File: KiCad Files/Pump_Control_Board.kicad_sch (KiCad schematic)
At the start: 70 parts, among them J1 OLED, J2 Conn_01x06, J3 USB_C_Receptacle_USB2.0, J4 Jack, M1 Stepper_Motor_bipolar, Q1 SSM3J328R, SW1 SW_USER, SW2 SW_RESET, U1 ESDALD05, U2 SN74LV1T34DCK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

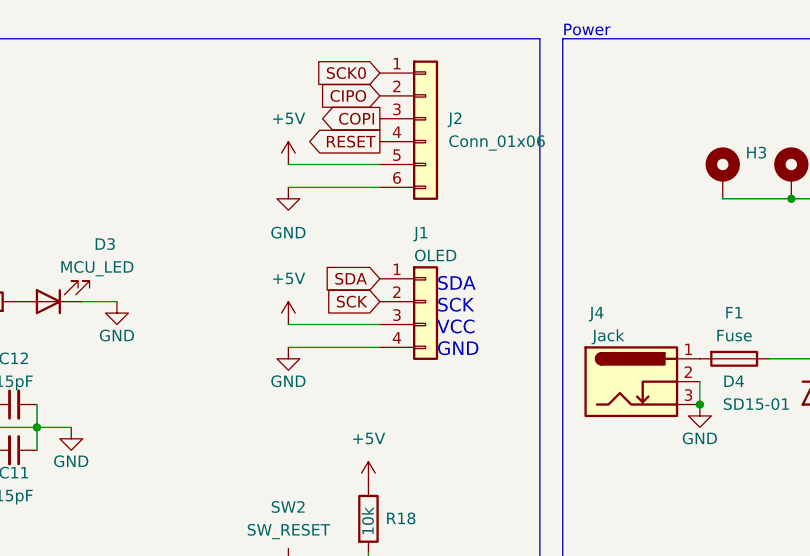
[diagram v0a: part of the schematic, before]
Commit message: Named ICP Header
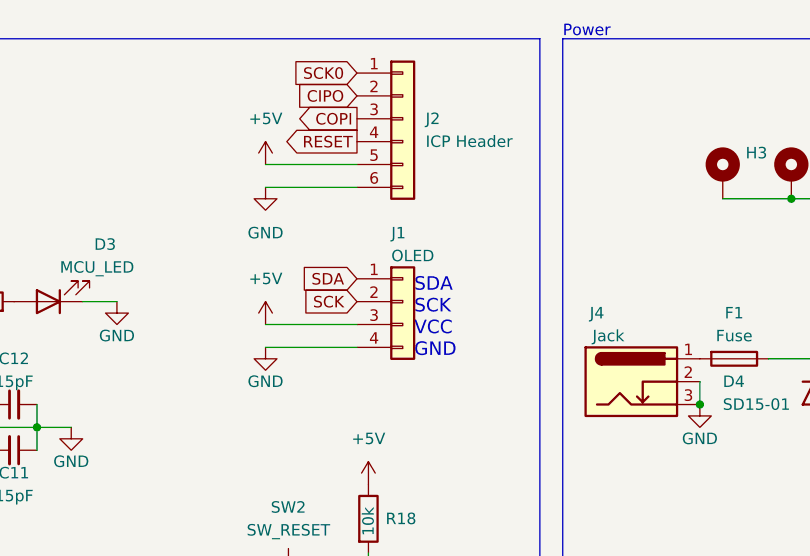
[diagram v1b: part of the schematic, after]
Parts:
- J2: value Conn_01x06 -> ICP Header
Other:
- moved on the sheet: J1, J2
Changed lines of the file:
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@@
     (stroke (width 0) (type default))
   )
-  (wire (pts (xy 107.95 29.21) (xy 118.11 29.21))
+  (wire (pts (xy 105.41 29.21) (xy 115.57 29.21))
     (stroke (width 0) (type default))
   )
@@
     (stroke (width 0) (type default))
   )
-  (wire (pts (xy 107.95 31.75) (xy 118.11 31.75))
+  (wire (pts (xy 105.41 31.75) (xy 115.57 31.75))
     (stroke (width 0) (type default))
   )
@@
     (stroke (width 0) (type default))
   )
-  (wire (pts (xy 107.95 49.53) (xy 118.11 49.53))
+  (wire (pts (xy 105.41 49.53) (xy 115.57 49.53))
     (stroke (width 0) (type default))
   )
@@
     (stroke (width 0) (type default))
   )
-  (wire (pts (xy 107.95 46.99) (xy 118.11 46.99))
+  (wire (pts (xy 105.41 46.99) (xy 115.57 46.99))
     (stroke (width 0) (type default))
   )
@@
     (effects (font (size 5 5)) (justify left bottom))
   )
-  (text "SDA\nSCK\nVCC\nGND" (at 124.46 50.8 0)
+  (text "SDA\nSCK\nVCC\nGND" (at 121.92 50.8 0)
     (effects (font (size 1.5 1.5)) (justify left bottom))
   )
@@
     )
   )
-  (global_label "SCK0" (shape input) (at 118.11 19.05 180) (fields_autoplaced)
+  (global_label "SCK0" (shape input) (at 115.57 19.05 180) (fields_autoplaced)
     (effects (font (size 1.27 1.27)) (justify right))
-    (property "Intersheetrefs" "${INTERSHEET_REFS}" (at 110.1658 19.05 0)
+    (property "Intersheetrefs" "${INTERSHEET_REFS}" (at 107.6258 19.05 0)
       (effects (font (size 1.27 1.27)) (justify right) hide)
     )
@@
     )
   )
-  (global_label "CIPO" (shape input) (at 118.11 21.59 180) (fields_autoplaced)
+  (global_label "CIPO" (shape input) (at 115.57 21.59 180) (fields_autoplaced)
     (effects (font (size 1.27 1.27)) (justify right))
-    (property "Intersheetrefs" "${INTERSHEET_REFS}" (at 110.6495 21.59 0)
+    (property "Intersheetrefs" "${INTERSHEET_REFS}" (at 108.1095 21.59 0)
       (effects (font (size 1.27 1.27)) (justify right) hide)
     )
@@
     )
   )
-  (global_label "SCK" (shape input) (at 118.11 44.45 180) (fields_autoplaced)
+  (global_label "SCK" (shape input) (at 115.57 44.45 180) (fields_autoplaced)
     (effects (font (size 1.27 1.27)) (justify right))
-    (property "Intersheetrefs" "${INTERSHEET_REFS}" (at 111.3753 44.45 0)
+    (property "Intersheetrefs" "${INTERSHEET_REFS}" (at 108.8353 44.45 0)
       (effects (font (size 1.27 1.27)) (justify right) hide)
     )
   )
-  (global_label "COPI" (shape output) (at 118.11 24.13 180) (fields_autoplaced)
+  (global_label "COPI" (shape output) (at 115.57 24.13 180) (fields_autoplaced)
     (effects (font (size 1.27 1.27)) (justify right))
-    (property "Intersheetrefs" "${INTERSHEET_REFS}" (at 110.6495 24.13 0)
+    (property "Intersheetrefs" "${INTERSHEET_REFS}" (at 108.1095 24.13 0)
       (effects (font (size 1.27 1.27)) (justify right) hide)
     )
@@
     )
   )
-  (global_label "RESET" (shape output) (at 118.11 26.67 180) (fields_autoplaced)
+  (global_label "RESET" (shape output) (at 115.57 26.67 180) (fields_autoplaced)
     (effects (font (size 1.27 1.27)) (justify right))
-    (property "Intersheetrefs" "${INTERSHEET_REFS}" (at 109.3797 26.67 0)
+    (property "Intersheetrefs" "${INTERSHEET_REFS}" (at 106.8397 26.67 0)
       (effects (font (size 1.27 1.27)) (justify right) hide)
     )
   )
-  (global_label "SDA" (shape input) (at 118.11 41.91 180) (fields_autoplaced)
+  (global_label "SDA" (shape input) (at 115.57 41.91 180) (fields_autoplaced)
     (effects (font (size 1.27 1.27)) (justify right))
-    (property "Intersheetrefs" "${INTERSHEET_REFS}" (at 111.5567 41.91 0)
+    (property "Intersheetrefs" "${INTERSHEET_REFS}" (at 109.0167 41.91 0)
       (effects (font (size 1.27 1.27)) (justify right) hide)
     )
@@
     )
   )
-  (symbol (lib_id "power:GND") (at 107.95 49.53 0) (unit 1)
+  (symbol (lib_id "power:GND") (at 105.41 49.53 0) (unit 1)
     (in_bom yes) (on_board yes) (dnp no)
-    (property "Reference" "#PWR021" (at 107.95 55.88 0)
+    (property "Reference" "#PWR021" (at 105.41 55.88 0)
       (effects (font (size 1.27 1.27)) hide)
     )
-    (property "Value" "GND" (at 107.95 53.34 0)
+    (property "Value" "GND" (at 105.41 53.34 0)
       (effects (font (size 1.27 1.27)))
     )
-    (property "Footprint" "" (at 107.95 49.53 0)
+    (property "Footprint" "" (at 105.41 49.53 0)
       (effects (font (size 1.27 1.27)) hide)
     )
-    (property "Datasheet" "" (at 107.95 49.53 0)
+    (property "Datasheet" "" (at 105.41 49.53 0)
       (effects (font (size 1.27 1.27)) hide)
     )
@@
     )
   )
-  (symbol (lib_id "Connector_Generic:Conn_01x06") (at 123.19 24.13 0) (unit 1)
+  (symbol (lib_id "Connector_Generic:Conn_01x06") (at 120.65 24.13 0) (unit 1)
     (in_bom yes) (on_board yes) (dnp no) (fields_autoplaced)
-    (property "Reference" "J2" (at 125.73 24.13 0)
+    (property "Reference" "J2" (at 123.19 24.13 0)
       (effects (font (size 1.27 1.27)) (justify left))
     )
-    (property "Value" "Conn_01x06" (at 125.73 26.67 0)
+    (property "Value" "ICP Header" (at 123.19 26.67 0)
       (effects (font (size 1.27 1.27)) (justify left))
     )
-    (property "Footprint" "Connector_PinHeader_2.54mm:PinHeader_1x06_P2.54mm_Vertical" (at 123.19 24.13 0)
+    (property "Footprint" "Connector_PinHeader_2.54mm:PinHeader_1x06_P2.54mm_Vertical" (at 120.65 24.13 0)
       (effects (font (size 1.27 1.27)) hide)
     )
-    (property "Datasheet" "~" (at 123.19 24.13 0)
+    (property "Datasheet" "~" (at 120.65 24.13 0)
       (effects (font (size 1.27 1.27)) hide)
     )
@@
     )
   )
-  (symbol (lib_id "power:GND") (at 107.95 31.75 0) (unit 1)
+  (symbol (lib_id "power:GND") (at 105.41 31.75 0) (unit 1)
     (in_bom yes) (on_board yes) (dnp no) (fields_autoplaced)
-    (property "Reference" "#PWR019" (at 107.95 38.1 0)
+    (property "Reference" "#PWR019" (at 105.41 38.1 0)
       (effects (font (size 1.27 1.27)) hide)
     )
-    (property "Value" "GND" (at 107.95 36.83 0)
+    (property "Value" "GND" (at 105.41 36.83 0)
       (effects (font (size 1.27 1.27)))
     )
-    (property "Footprint" "" (at 107.95 31.75 0)
+    (property "Footprint" "" (at 105.41 31.75 0)
       (effects (font (size 1.27 1.27)) hide)
     )
-    (property "Datasheet" "" (at 107.95 31.75 0)
+    (property "Datasheet" "" (at 105.41 31.75 0)
       (effects (font (size 1.27 1.27)) hide)
     )
@@
     )
   )
-  (symbol (lib_id "Connector_Generic:Conn_01x04") (at 123.19 44.45 0) (unit 1)
+  (symbol (lib_id "Connector_Generic:Conn_01x04") (at 120.65 44.45 0) (unit 1)
     (in_bom yes) (on_board yes) (dnp no)
-    (property "Reference" "J1" (at 121.92 36.83 0)
+    (property "Reference" "J1" (at 119.38 36.83 0)
       (effects (font (size 1.27 1.27)) (justify left))
     )
-    (property "Value" "OLED" (at 121.92 39.37 0)
+    (property "Value" "OLED" (at 119.38 39.37 0)
       (effects (font (size 1.27 1.27)) (justify left))
     )
-    (property "Footprint" "Connector_PinSocket_2.54mm:PinSocket_1x04_P2.54mm_Vertical" (at 123.19 44.45 0)
+    (property "Footprint" "Connector_PinSocket_2.54mm:PinSocket_1x04_P2.54mm_Vertical" (at 120.65 44.45 0)
       (effects (font (size 1.27 1.27)) hide)
     )
-    (property "Datasheet" "~" (at 123.19 44.45 0)
+    (property "Datasheet" "~" (at 120.65 44.45 0)
       (effects (font (size 1.27 1.27)) hide)
     )
@@
     )
   )
-  (symbol (lib_id "power:+5V") (at 107.95 29.21 0) (unit 1)
+  (symbol (lib_id "power:+5V") (at 105.41 29.21 0) (unit 1)
     (in_bom yes) (on_board yes) (dnp no) (fields_autoplaced)
-    (property "Reference" "#PWR018" (at 107.95 33.02 0)
+    (property "Reference" "#PWR018" (at 105.41 33.02 0)
       (effects (font (size 1.27 1.27)) hide)
     )
-    (property "Value" "+5V" (at 107.95 24.13 0)
+    (property "Value" "+5V" (at 105.41 24.13 0)
       (effects (font (size 1.27 1.27)))
     )
-    (property "Footprint" "" (at 107.95 29.21 0)
+    (property "Footprint" "" (at 105.41 29.21 0)
       (effects (font (size 1.27 1.27)) hide)
     )
-    (property "Datasheet" "" (at 107.95 29.21 0)
+    (property "Datasheet" "" (at 105.41 29.21 0)
       (effects (font (size 1.27 1.27)) hide)
     )
@@
     )
   )
-  (symbol (lib_id "power:+5V") (at 107.95 46.99 0) (unit 1)
+  (symbol (lib_id "power:+5V") (at 105.41 46.99 0) (unit 1)
     (in_bom yes) (on_board yes) (dnp no) (fields_autoplaced)
-    (property "Reference" "#PWR020" (at 107.95 50.8 0)
+    (property "Reference" "#PWR020" (at 105.41 50.8 0)
       (effects (font (size 1.27 1.27)) hide)
     )
-    (property "Value" "+5V" (at 107.95 41.91 0)
+    (property "Value" "+5V" (at 105.41 41.91 0)
       (effects (font (size 1.27 1.27)))
     )
-    (property "Footprint" "" (at 107.95 46.99 0)
+    (property "Footprint" "" (at 105.41 46.99 0)
       (effects (font (size 1.27 1.27)) hide)
     )
-    (property "Datasheet" "" (at 107.95 46.99 0)
+    (property "Datasheet" "" (at 105.41 46.99 0)
       (effects (font (size 1.27 1.27)) hide)
     )
